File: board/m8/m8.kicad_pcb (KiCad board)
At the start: 2 copper layers, 50 x 25 mm, 11 parts, among them J1 program, SW1 B3F-4000, U1 CH32V003f4p6

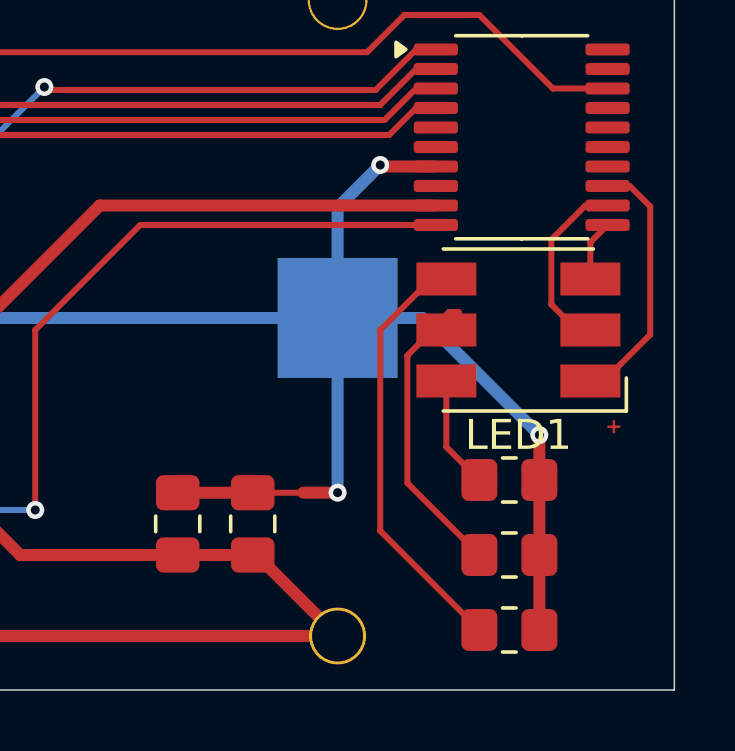
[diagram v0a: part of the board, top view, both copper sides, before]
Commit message: moved all power lines to 0.4mm
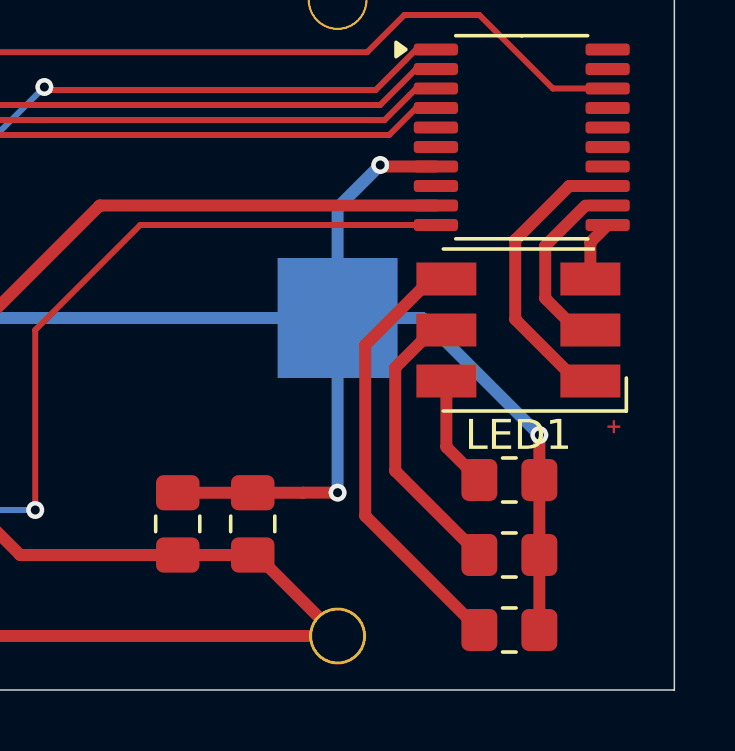
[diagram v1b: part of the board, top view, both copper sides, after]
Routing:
- net Net-(LED1-BA): track 8.61 -> 10.3 mm
- net Net-(LED1-RK): track 12.2 -> 10.8 mm
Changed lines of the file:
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@@
 		(start 162.203616 116.9)
 		(end 163.303616 118)
-		(width 0.2)
+		(width 0.4)
 		(layer "F.Cu")
 		(net 1)
@@
 		(start 162.203616 114.7)
 		(end 162.203616 116.9)
-		(width 0.2)
+		(width 0.4)
 		(layer "F.Cu")
 		(net 1)
@@
 		(start 167.003616 110.075)
 		(end 167.003616 111.3)
-		(width 0.2)
+		(width 0.4)
 		(layer "F.Cu")
 		(net 2)
@@
 		(start 167.578616 109.5)
 		(end 167.003616 110.075)
-		(width 0.2)
+		(width 0.4)
 		(layer "F.Cu")
 		(net 2)
-	)
-	(segment
-		(start 169 113.153616)
-		(end 169 108.883885)
-		(width 0.2)
-		(layer "F.Cu")
-		(net 3)
-	)
-	(segment
-		(start 168.316115 108.2)
-		(end 167.578616 108.2)
-		(width 0.2)
-		(layer "F.Cu")
-		(net 3)
 	)
 	(segment
@@
 	)
 	(segment
-		(start 167.453616 114.7)
-		(end 169 113.153616)
-		(width 0.2)
-		(layer "F.Cu")
-		(net 3)
-	)
-	(segment
-		(start 169 108.883885)
-		(end 168.316115 108.2)
-		(width 0.2)
-		(layer "F.Cu")
-		(net 3)
-	)
-	(segment
-		(start 166.553616 113)
-		(end 165.703616 112.15)
-		(width 0.2)
-		(layer "F.Cu")
-		(net 4)
+		(start 166.3 108.2)
+		(end 167.578616 108.2)
+		(width 0.4)
+		(layer "F.Cu")
+		(net 3)
+	)
+	(segment
+		(start 167.003616 114.7)
+		(end 166.553616 114.7)
+		(width 0.2)
+		(layer "F.Cu")
+		(net 3)
+	)
+	(segment
+		(start 164.5 112.646384)
+		(end 164.5 110)
+		(width 0.4)
+		(layer "F.Cu")
+		(net 3)
+	)
+	(segment
+		(start 164.5 110)
+		(end 166.3 108.2)
+		(width 0.4)
+		(layer "F.Cu")
+		(net 3)
+	)
+	(segment
+		(start 166.553616 114.7)
+		(end 164.5 112.646384)
+		(width 0.4)
+		(layer "F.Cu")
+		(net 3)
 	)
 	(segment
@@
 	)
 	(segment
-		(start 165.703616 109.987501)
+		(start 165.5 110.191117)
 		(end 166.841117 108.85)
-		(width 0.2)
+		(width 0.4)
 		(layer "F.Cu")
 		(net 4)
@@
 	)
 	(segment
+		(start 166.553616 113)
+		(end 165.5 111.946384)
+		(width 0.4)
+		(layer "F.Cu")
+		(net 4)
+	)
+	(segment
+		(start 165.5 111.946384)
+		(end 165.5 110.191117)
+		(width 0.4)
+		(layer "F.Cu")
+		(net 4)
+	)
+	(segment
 		(start 166.128616 113)
 		(end 167.803616 113)
@@
 	)
 	(segment
-		(start 165.703616 112.15)
-		(end 165.703616 109.987501)
-		(width 0.2)
-		(layer "F.Cu")
-		(net 4)
-	)
-	(segment
-		(start 162.628616 112.4)
-		(end 162.296322 112.4)
-		(width 0.2)
-		(layer "F.Cu")
-		(net 5)
-	)
-	(segment
-		(start 162.296322 112.4)
-		(end 161.303616 113.392706)
-		(width 0.2)
+		(start 160.5 117.696384)
+		(end 160.5 114.253616)
+		(width 0.4)
+		(layer "F.Cu")
+		(net 5)
+	)
+	(segment
+		(start 163.303616 120.5)
+		(end 160.5 117.696384)
+		(width 0.4)
 		(layer "F.Cu")
 		(net 5)
@@
 	)
 	(segment
-		(start 163.303616 120.5)
-		(end 160.903616 118.1)
-		(width 0.2)
+		(start 160.5 114.253616)
+		(end 161.753616 113)
+		(width 0.4)
 		(layer "F.Cu")
 		(net 5)
@@
 	)
 	(segment
-		(start 160.903616 113.85)
-		(end 161.753616 113)
-		(width 0.2)
-		(layer "F.Cu")
-		(net 5)
-	)
-	(segment
-		(start 160.903616 118.1)
-		(end 160.903616 113.85)
-		(width 0.2)
-		(layer "F.Cu")
-		(net 5)
-	)
-	(segment
 		(start 162.353616 113)
 		(end 162.053616 113.3)
@@
 	(segment
 		(start 163.303616 123)
-		(end 160 119.696384)
-		(width 0.2)
+		(end 159.5 119.196384)
+		(width 0.4)
+		(layer "F.Cu")
+		(net 6)
+	)
+	(segment
+		(start 159.5 113.5)
+		(end 161.7 111.3)
+		(width 0.4)
 		(layer "F.Cu")
 		(net 6)
@@
 	)
 	(segment
-		(start 160 113)
-		(end 161.7 111.3)
-		(width 0.2)
-		(layer "F.Cu")
-		(net 6)
-	)
-	(segment
-		(start 160 119.696384)
-		(end 160 113)
-		(width 0.2)
+		(start 159.5 119.196384)
+		(end 159.5 113.5)
+		(width 0.4)
 		(layer "F.Cu")
 		(net 6)
@@
 		(start 157.425 118.425)
 		(end 155.75 118.425)
-		(width 0.2)
-		(layer "F.Cu")
-		(net 8)
+		(width 0.4)
+		(layer "F.Cu")
+		(net 8)

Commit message: cosmetic changes
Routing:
- net VCC: track 116.6 -> 117.9 mm
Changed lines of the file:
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@@
+	)
+	(segment
+		(start 143.5 101)
+		(end 131 101)
+		(width 0.4)
+		(layer "F.Cu")
+		(net 17)
 	)
 	(segment
@@
 		(start 148 120.5)
 		(end 147 119.5)
-		(width 0.4)
-		(layer "F.Cu")
-		(net 17)
-	)
-	(segment
-		(start 131.5 101)
-		(end 130.5 102)
-		(width 0.4)
-		(layer "F.Cu")
-		(net 17)
-	)
-	(segment
-		(start 143.5 101)
-		(end 131.5 101)
 		(width 0.4)
 		(layer "F.Cu")
@@
 	)
 	(segment
-		(start 130.7 123.2)
-		(end 158.578616 123.2)
+		(start 150.65 108.85)
+		(end 161.853616 108.85)
 		(width 0.4)
 		(layer "F.Cu")
@@
 	)
 	(segment
-		(start 150.65 108.85)
-		(end 161.853616 108.85)
+		(start 130.5 101.5)
+		(end 130.5 123.5)
 		(width 0.4)
 		(layer "F.Cu")
@@
 	)
 	(segment
+		(start 131 124)
+		(end 157.778616 124)
+		(width 0.4)
+		(layer "F.Cu")
+		(net 17)
+	)
+	(segment
 		(start 143.343616 103)
 		(end 143.343616 101.156384)
@@
 	)
 	(segment
-		(start 130.5 123)
-		(end 130.7 123.2)
+		(start 130.5 123.5)
+		(end 131 124)
+		(width 0.4)
+		(layer "F.Cu")
+		(net 17)
+	)
+	(segment
+		(start 131 101)
+		(end 130.5 101.5)
+		(width 0.4)
+		(layer "F.Cu")
+		(net 17)
+	)
+	(segment
+		(start 157.778616 124)
+		(end 158.578616 123.2)
 		(width 0.4)
 		(layer "F.Cu")
@@
 		(width 0.4)
 		(layer "F.Cu")
-		(net 17)
-	)
-	(segment
-		(start 130.5 102)
-		(end 130.5 123)
-		(width 0.4)
-		(layer "F.Cu")
